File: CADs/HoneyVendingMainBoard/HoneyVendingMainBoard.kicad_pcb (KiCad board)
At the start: 2 copper layers, 31 parts, among them J1 SegmentPins, J2 CoinPins, J3 ConnToDoors, J4 12V Power, U1 L7805, U2 74HC165

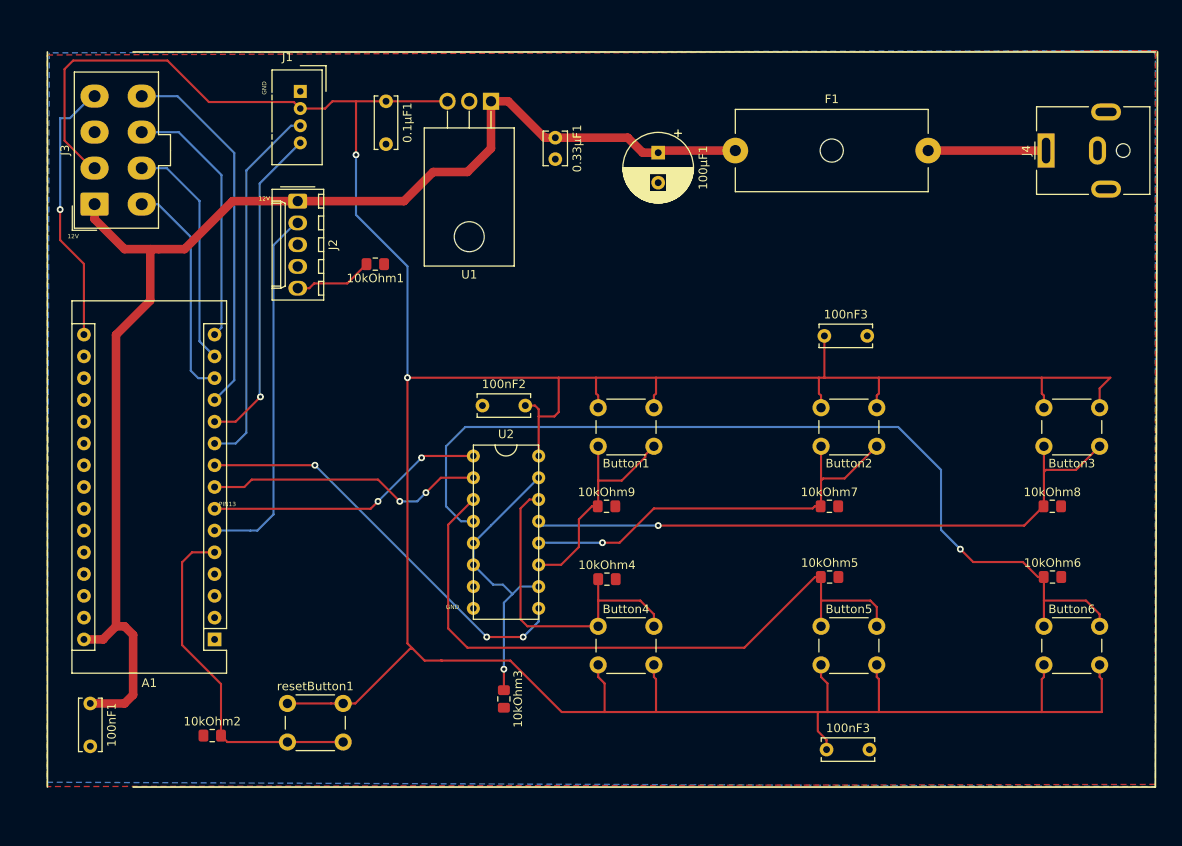
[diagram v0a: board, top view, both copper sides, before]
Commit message: Reworded PCBs and added PCB pdfs
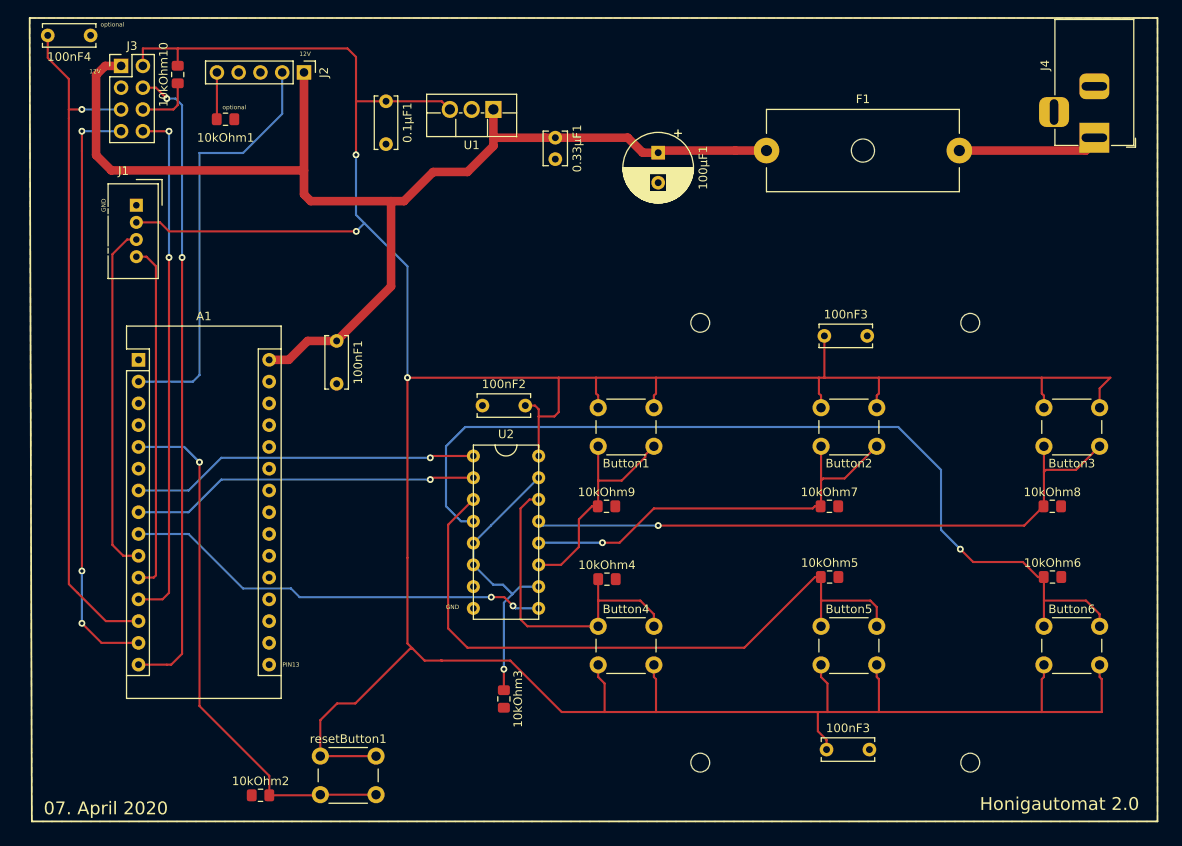
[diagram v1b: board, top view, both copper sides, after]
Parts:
- added 100nF4: RCLKAntiFlicker, Capacitor_THT:C_Disc_D6.0mm_W2.5mm_P5.00mm, F.Cu at (66.0, 36.1)
- added 10kOhm10: DoorClearPullUp, Resistor_SMD:R_0805_2012Metric_Pad1.15x1.40mm_HandSolder, F.Cu at (76.2, 40.6)
- added ?: MountingHole_2.2mm_M2_ISO14580, MountingHole:MountingHole_2.2mm_M2_ISO14580, F.Cu at (168.7, 120.9)
- added ?: MountingHole_2.2mm_M2_ISO14580, MountingHole:MountingHole_2.2mm_M2_ISO14580, F.Cu at (137.2, 120.9)
- added ?: MountingHole_2.2mm_M2_ISO14580, MountingHole:MountingHole_2.2mm_M2_ISO14580, F.Cu at (137.2, 69.6)
- added ?: MountingHole_2.2mm_M2_ISO14580, MountingHole:MountingHole_2.2mm_M2_ISO14580, F.Cu at (168.7, 69.6)
- 0.1µF1: value C -> VR3
- 0.33µF1: value C -> VR2
- 100nF1: value C -> ArduinoDecouple
- 100nF2: value C -> ButtonDecouple
- 100µF1: value C -> VR1
- 10kOhm1: value R -> CoinInhibitPullDown
- 10kOhm2: value R -> ResetPD
- 10kOhm4: value R -> ButtonR4
- 10kOhm5: value R -> ButtonR5
- 10kOhm6: value R -> ButtonR6
- 10kOhm7: value R -> ButtonR2
- 10kOhm8: value R -> ButtonR3
- 10kOhm9: value R -> ButtonR1
- J2: footprint Connector_Molex:Molex_KK-254_AE-6410-05A_1x05_P2.54mm_Vertical -> Connector_PinHeader_2.54mm:PinHeader_1x05_P2.54mm_Vertical
- J3: footprint Connector_Molex:Molex_Mini-Fit_Jr_5566-08A_2x04_P4.20mm_Vertical -> Connector_PinHeader_2.54mm:PinHeader_2x04_P2.54mm_Vertical
- J4: footprint Connector_BarrelJack:BarrelJack_CUI_PJ-063AH_Horizontal -> Connector_BarrelJack:BarrelJack_Horizontal
- U1: footprint Package_TO_SOT_THT:TO-220F-3_Horizontal_TabDown -> Package_TO_SOT_THT:TO-220F-3_Vertical
- moved 100nF1 51.1 mm to (94.7, 71.7)
- moved A1 33.8 mm to (71.6, 73.9), turned to 0 degrees
- moved 10kOhm1 24.3 mm to (81.8, 45.8)
- moved J1 23.3 mm to (71.4, 55.9)
- moved J3 16.4 mm to (69.6, 39.6), turned to 0 degrees
- moved J2 15.0 mm to (90.9, 40.4)
- moved 10kOhm2 8.96 mm to (85.9, 124.7)
- moved resetButton1 7.24 mm to (92.8, 120.1)
- moved J4 5.83 mm to (183.1, 48.0), turned to 270 degrees
- moved F1 3.64 mm to (144.9, 49.5)
- moved U1 0.99 mm to (113.0, 44.7)
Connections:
- net PISOClock renamed /PISOClock
- net PISOOutput renamed /PISOOutput
- net PISO_SL renamed /PISO_SL
- net doorRCLK renamed /doorRCLK
- net doorSER renamed /doorSER
- net segmentClock renamed /segmentClock
- net segmentSignal renamed /segmentSignal
- A1 pad 14: doorSRCLR -> /doorSRCLK
- A1 pad 15: doorSRCLK -> /doorOE
- A1 pad 16: DoorOE -> Net-(A1-Pad16)
- A1 pad 2: Net-(A1-Pad2) -> /CoinSerial
- A1 pad 6: CoinSerial -> Net-(A1-Pad6)
- J2 pad 2: CoinSerial -> /CoinSerial
- J3 pad 4: DoorOE -> /doorOE
- J3 pad 6: doorSRCLR -> Net-(10kOhm10-Pad1)
- J3 pad 7: doorSRCLK -> /doorSRCLK
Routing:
- net /doorOE: track 0.00 -> 75.0 mm, vias 0 -> 2
- net /doorSRCLK: track 0.00 -> 69.5 mm, vias 0 -> 3
- net /doorRCLK: track 26.1 -> 81.0 mm, vias 0 -> 1
- net /CoinSerial: track 0.00 -> 49.7 mm
- net CoinSerial: track 43.0 -> 0.00 mm
- net DoorOE: track 31.5 -> 0.00 mm, vias 1 -> 0
- net doorSRCLK: track 30.3 -> 0.00 mm
- net doorSRCLR: track 27.2 -> 0.00 mm
- net Net-(10kOhm2-Pad2): track 40.9 -> 62.6 mm, vias 0 -> 1
- net +5V: track 389.8 -> 409.9 mm, vias 2 -> 3
- net /doorSER: track 43.3 -> 60.8 mm, vias 0 -> 2
- net /12VFused: track 155.8 -> 141.7 mm
- net /PISOClock: track 32.7 -> 40.7 mm, vias 2 -> 1
- net /PISO_SL: track 32.7 -> 40.7 mm, vias 2 -> 1
- net Net-(10kOhm10-Pad1): track 0.00 -> 6.81 mm
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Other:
- board text added: "07. April 2020"
- board text added: "Honigautomat 2.0"
- board text added: "optional"

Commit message: Applying nicos feedback for boards
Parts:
- removed 100nF4: RCLKAntiFlicker, Capacitor_THT:C_Disc_D6.0mm_W2.5mm_P5.00mm
- added J5: Power Line, Connector_PinHeader_2.54mm:PinHeader_1x02_P2.54mm_Vertical, F.Cu at (86.1, 54.7)
- moved 10kOhm3 2.50 mm to (111.8, 113.3)
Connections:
- J3 pad 1: /12VFused -> Net-(J3-Pad1)
- J3 pad 2: +5V -> Net-(J3-Pad2)
- J3 pad 3: GND -> +5V
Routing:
- net +5V: track 409.9 -> 550.8 mm
- net /12VFused: track 141.7 -> 109.3 mm
- net /doorRCLK: track 81.0 -> 71.4 mm
- net Net-(10kOhm6-Pad1): track 107.3 -> 98.7 mm
- net Net-(10kOhm9-Pad1): track 26.9 -> 18.6 mm
- net Net-(10kOhm7-Pad1): track 49.8 -> 41.7 mm
- net Net-(10kOhm8-Pad1): track 74.8 -> 67.5 mm
- net Net-(10kOhm5-Pad1): track 78.9 -> 86.1 mm
- net Net-(10kOhm2-Pad2): track 62.6 -> 56.1 mm
- net Net-(10kOhm3-Pad1): track 34.3 -> 35.2 mm
- net Net-(10kOhm4-Pad1): track 39.0 -> 38.4 mm
- net GND: vias 0 -> 5
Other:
- board text added: "5V"

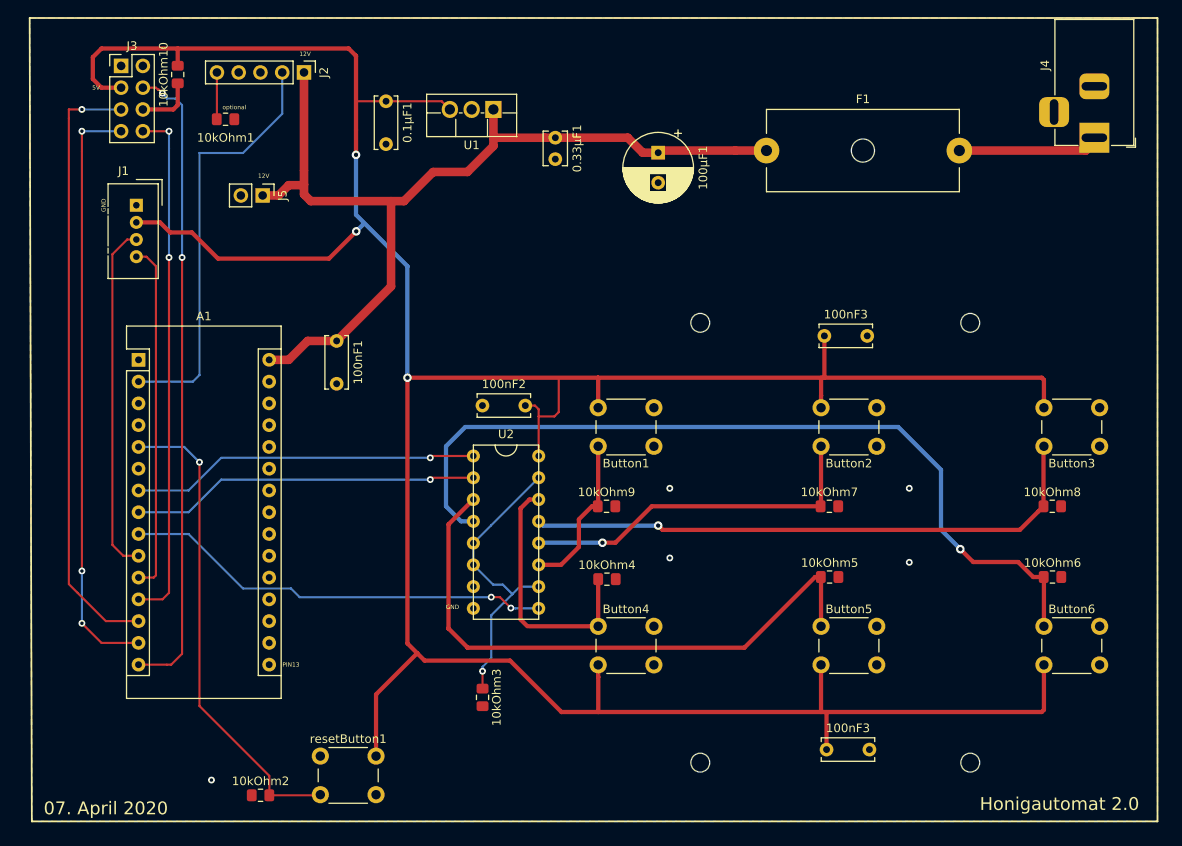
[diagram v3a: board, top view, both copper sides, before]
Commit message: Split Main Board into Main Board and Button Board
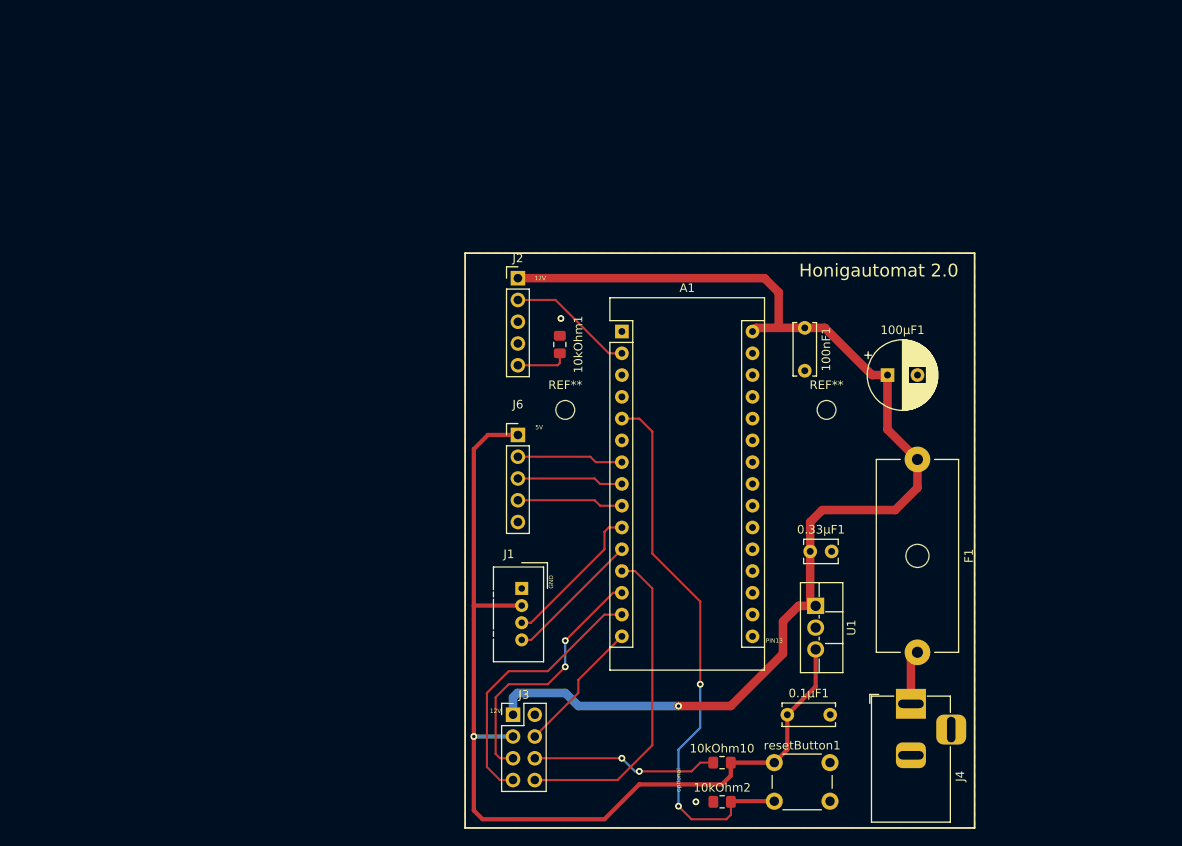
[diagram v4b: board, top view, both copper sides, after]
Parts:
- removed 100nF2: ButtonDecouple, Capacitor_THT:C_Disc_D6.0mm_W2.5mm_P5.00mm
- removed 100nF3 (x2): ButtonC, Capacitor_THT:C_Disc_D6.0mm_W2.5mm_P5.00mm
- removed 10kOhm3: R, Resistor_SMD:R_0805_2012Metric_Pad1.15x1.40mm_HandSolder
- removed 10kOhm4: ButtonR4, Resistor_SMD:R_0805_2012Metric_Pad1.15x1.40mm_HandSolder
- removed 10kOhm5: ButtonR5, Resistor_SMD:R_0805_2012Metric_Pad1.15x1.40mm_HandSolder
- removed 10kOhm6: ButtonR6, Resistor_SMD:R_0805_2012Metric_Pad1.15x1.40mm_HandSolder
- removed 10kOhm7: ButtonR2, Resistor_SMD:R_0805_2012Metric_Pad1.15x1.40mm_HandSolder
- removed 10kOhm8: ButtonR3, Resistor_SMD:R_0805_2012Metric_Pad1.15x1.40mm_HandSolder
- removed 10kOhm9: ButtonR1, Resistor_SMD:R_0805_2012Metric_Pad1.15x1.40mm_HandSolder
- removed ? (x4): MountingHole_2.2mm_M2_ISO14580, MountingHole:MountingHole_2.2mm_M2_ISO14580
- removed Button1, Button2, Button3, Button4, Button5, Button6: SW_DPST_x2, Button_Switch_THT:SW_PUSH_6mm_H9.5mm
- removed J5: Power Line, Connector_PinHeader_2.54mm:PinHeader_1x02_P2.54mm_Vertical
- removed U2: 74HC165, Customs:74HC165
- added J6: Conn_01x05_Male, Connector_PinHeader_2.54mm:PinHeader_1x05_P2.54mm_Vertical, F.Cu at (115.9, 82.7)
- added REF**: MountingHole_2.2mm_M2_ISO14580, MountingHole:MountingHole_2.2mm_M2_ISO14580, F.Cu at (151.9, 79.8)
- added REF**: MountingHole_2.2mm_M2_ISO14580, MountingHole:MountingHole_2.2mm_M2_ISO14580, F.Cu at (121.4, 79.8)
- moved 10kOhm10 102.4 mm to (139.7, 120.9), turned to 0 degrees
- moved J3 88.4 mm to (115.3, 115.3)
- moved 0.1µF1 85.5 mm to (147.3, 115.3), turned to 0 degrees
- moved J4 69.4 mm to (161.7, 114.0), turned to 90 degrees
- moved U1 69.0 mm to (150.6, 102.6), turned to 270 degrees
- moved J1 63.4 mm to (116.3, 100.6)
- moved 0.33µF1 56.7 mm to (150.0, 96.3), turned to 0 degrees
- moved A1 56.5 mm to (128.0, 70.6)
- moved 100nF1 54.6 mm to (149.4, 70.2)
- moved 10kOhm2 53.9 mm to (139.7, 125.5)
- moved resetButton1 53.0 mm to (145.8, 120.9)
- moved 10kOhm1 47.0 mm to (120.8, 72.1), turned to 270 degrees
- moved F1 40.1 mm to (162.5, 85.5), turned to 270 degrees
- moved 100µF1 37.3 mm to (159.0, 75.7), turned to 0 degrees
- moved J2 34.6 mm to (115.9, 64.4), turned to 0 degrees
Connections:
- J3 pad 1: Net-(J3-Pad1) -> /12VFused
- J3 pad 2: Net-(J3-Pad2) -> GND
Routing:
- net +5V: track 550.8 -> 112.5 mm, vias 3 -> 1
- net Net-(10kOhm6-Pad1): track 98.7 -> 0.00 mm, vias 1 -> 0
- net Net-(10kOhm5-Pad1): track 86.1 -> 0.00 mm
- net Net-(10kOhm8-Pad1): track 67.5 -> 0.00 mm, vias 1 -> 0
- net /doorOE: track 75.1 -> 15.9 mm, vias 2 -> 0
- net Net-(10kOhm7-Pad1): track 41.7 -> 0.00 mm, vias 1 -> 0
- net /doorRCLK: track 71.4 -> 30.4 mm, vias 1 -> 2
- net Net-(10kOhm4-Pad1): track 38.4 -> 0.00 mm
- net /PISOOutput: track 50.3 -> 12.4 mm, vias 2 -> 0
- net /doorSRCLK: track 69.5 -> 31.9 mm, vias 3 -> 0
- net Net-(10kOhm3-Pad1): track 35.2 -> 0.00 mm, vias 1 -> 0
- net /CoinSerial: track 49.7 -> 14.7 mm
- net /PISOClock: track 40.7 -> 12.4 mm, vias 1 -> 0
- net /PISO_SL: track 40.7 -> 12.4 mm, vias 1 -> 0
- net /12VFused: track 109.3 -> 137.5 mm, vias 0 -> 1
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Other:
- board text removed: "07. April 2020"
